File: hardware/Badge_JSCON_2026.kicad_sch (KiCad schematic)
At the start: 38 parts, among them J2 LCD, P1 USB_C_Plug_USB2.0, Q2 BC846, SW3 ON, U1 ESP32-S3-WROOM-1-N8, U2 BL8072CLTR33, U5 VGdd79S915N0S1

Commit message: feat(Hw):Update_Files
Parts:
- SW1, SW2, SW4, SW5, SW6, SW7: value (none) -> ~
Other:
- note added: "ESP32-C6"
- note removed: "ESP32-S3"

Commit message: feat(Hw):Init_Floorplan
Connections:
- net CS2: no longer names the net of U1.22 (IO14)
- net IO0: no longer names the net of U1.6 (IO6)
- net IO1: no longer names the net of U1.7 (IO7)
- net IO2: no longer names the net of U1.5 (IO5)
- net IRQ: no longer names the net of U1.12 (IO8)
- net MISO2: no longer names the net of U1.10 (IO17)
- net MOSI2: no longer names the net of U1.9 (IO16)
- net SCK2: no longer names the net of U1.8 (IO15)
- net SCL1: no longer names the net of U1.34 (IO41)
- net SDA1: no longer names the net of U1.35 (IO42)
- net SDN: no longer names the net of U1.4 (IO4)
- no-connect marks 5 -> 16
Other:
- company: (none) -> Electronic Cats
- title: (none) -> Badge JSCON 2026
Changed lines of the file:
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@@
 	(generator_version "9.0")
 	(paper "A3")
+	(title_block
+		(title "Badge JSCON 2026")
+		(rev "v1.0")
+		(company "Electronic Cats")
+		(comment 1 "Lizeth Gallegos Martínez")
+	)
 	(text "VGdd79S915N0S1\n"
 		(exclude_from_sim no)
@@
 	)
 	(no_connect
+		(at 36.83 45.72)
+	)
+	(no_connect
 		(at 36.83 71.12)
+	)
+	(no_connect
+		(at 36.83 48.26)
+	)
+	(no_connect
+		(at 77.47 68.58)
 	)
 	(no_connect
@@
 	)
 	(no_connect
+		(at 36.83 40.64)
+	)
+	(no_connect
+		(at 36.83 43.18)
+	)
+	(no_connect
+		(at 36.83 60.96)
+	)
+	(no_connect
+		(at 36.83 86.36)
+	)
+	(no_connect
+		(at 36.83 55.88)
+	)
+	(no_connect
+		(at 36.83 53.34)
+	)
+	(no_connect
 		(at 77.47 91.44)
 	)
@@
 		(at 331.47 68.58)
 	)
+	(no_connect
+		(at 36.83 50.8)
+	)
+	(no_connect
+		(at 77.47 71.12)
+	)
 	(wire
 		(pts
@@
 	(wire
 		(pts
-			(xy 81.28 68.58) (xy 77.47 68.58)
-		)
-		(stroke
-			(width 0)
-			(type default)
-		)
-	)
-	(wire
-		(pts
-			(xy 78.74 76.2) (xy 77.47 76.2)
+			(xy 80.01 76.2) (xy 77.47 76.2)
 		)
 		(stroke
@@
 	(wire
 		(pts
-			(xy 35.56 43.18) (xy 36.83 43.18)
-		)
-		(stroke
-			(width 0)
-			(type default)
-		)
-	)
-	(wire
-		(pts
 			(xy 340.36 55.88) (xy 340.36 58.42)
 		)
@@
 	(wire
 		(pts
-			(xy 36.83 86.36) (xy 33.02 86.36)
-		)
-		(stroke
-			(width 0)
-			(type default)
-		)
-	)
-	(wire
-		(pts
 			(xy 68.58 142.24) (xy 68.58 144.78)
 		)
@@
 	(wire
 		(pts
-			(xy 33.02 60.96) (xy 36.83 60.96)
-		)
-		(stroke
-			(width 0)
-			(type default)
-		)
-	)
-	(wire
-		(pts
 			(xy 156.21 57.15) (xy 152.019 57.15)
 		)
@@
 	(wire
 		(pts
-			(xy 35.56 45.72) (xy 36.83 45.72)
-		)
-		(stroke
-			(width 0)
-			(type default)
-		)
-	)
-	(wire
-		(pts
 			(xy 205.74 49.53) (xy 203.962 49.53)
 		)
@@
 	(wire
 		(pts
-			(xy 33.02 40.64) (xy 36.83 40.64)
-		)
-		(stroke
-			(width 0)
-			(type default)
-		)
-	)
-	(wire
-		(pts
 			(xy 33.02 66.04) (xy 36.83 66.04)
 		)
@@
 	(wire
 		(pts
-			(xy 81.28 71.12) (xy 77.47 71.12)
-		)
-		(stroke
-			(width 0)
-			(type default)
-		)
-	)
-	(wire
-		(pts
 			(xy 106.68 243.84) (xy 104.14 243.84)
 		)
@@
 	(wire
 		(pts
-			(xy 35.56 48.26) (xy 36.83 48.26)
-		)
-		(stroke
-			(width 0)
-			(type default)
-		)
-	)
-	(wire
-		(pts
 			(xy 128.27 68.834) (xy 128.27 72.644)
 		)
@@
 	(wire
 		(pts
-			(xy 33.02 50.8) (xy 36.83 50.8)
-		)
-		(stroke
-			(width 0)
-			(type default)
-		)
-	)
-	(wire
-		(pts
 			(xy 59.69 144.78) (xy 60.96 144.78)
 		)
@@
 	(wire
 		(pts
-			(xy 33.02 55.88) (xy 36.83 55.88)
-		)
-		(stroke
-			(width 0)
-			(type default)
-		)
-	)
-	(wire
-		(pts
 			(xy 44.45 176.53) (xy 44.45 177.292)
 		)
@@
 	(wire
 		(pts
-			(xy 33.02 53.34) (xy 36.83 53.34)
-		)
-		(stroke
-			(width 0)
-			(type default)
-		)
-	)
-	(wire
-		(pts
 			(xy 25.4 33.02) (xy 36.83 33.02)
 		)
@@
 	(wire
 		(pts
-			(xy 78.74 73.66) (xy 77.47 73.66)
+			(xy 80.01 73.66) (xy 77.47 73.66)
 		)
 		(stroke
@@
 		)
 	)
-	(label "SCK2"
-		(at 33.02 50.8 180)
-		(effects
-			(font
-				(size 1.27 1.27)
-			)
-			(justify right bottom)
-		)
-	)
 	(label "BUSY"
-		(at 78.74 76.2 0)
+		(at 80.01 76.2 0)
 		(effects
 			(font
@@
 		)
 	)
-	(label "CS2"
-		(at 33.02 86.36 180)
-		(effects
-			(font
-				(size 1.27 1.27)
-			)
-			(justify right bottom)
-		)
-	)
 	(label "RIGHT"
 		(at 201.93 49.53 180)
@@
 		)
 	)
-	(label "IO0"
-		(at 35.56 45.72 180)
-		(effects
-			(font
-				(size 1.27 1.27)
-			)
-			(justify right bottom)
-		)
-	)
 	(label "MISO"
 		(at 81.28 83.82 0)
@@
 	)
 	(label "UP"
-		(at 78.74 73.66 0)
+		(at 80.01 73.66 0)
 		(effects
 			(font
@@
 		)
 	)
-	(label "IRQ"
-		(at 33.02 60.96 180)
-		(effects
-			(font
-				(size 1.27 1.27)
-			)
-			(justify right bottom)
-		)
-	)
 	(label "SCL"
 		(at 104.14 246.38 180)
@@
 		)
 	)
-	(label "MOSI2"
-		(at 33.02 53.34 180)
-		(effects
-			(font
-				(size 1.27 1.27)
-			)
-			(justify right bottom)
-		)
-	)
 	(label "DOWN"
 		(at 78.74 63.5 0)
@@
 		)
 	)
-	(label "IO1"
-		(at 35.56 48.26 180)
-		(effects
-			(font
-				(size 1.27 1.27)
-			)
-			(justify right bottom)
-		)
-	)
-	(label "SDN"
-		(at 33.02 40.64 180)
-		(effects
-			(font
-				(size 1.27 1.27)
-			)
-			(justify right bottom)
-		)
-	)
 	(label "SDA"
 		(at 35.56 243.84 180)
@@
 		)
 	)
-	(label "IO2"
-		(at 35.56 43.18 180)
-		(effects
-			(font
-				(size 1.27 1.27)
-			)
-			(justify right bottom)
-		)
-	)
-	(label "MISO2"
-		(at 33.02 55.88 180)
-		(effects
-			(font
-				(size 1.27 1.27)
-			)
-			(justify right bottom)
-		)
-	)
 	(label "D-"
 		(at 63.246 149.86 0)
@@
 		)
 	)
-	(label "SDA1"
-		(at 81.28 68.58 0)
-		(effects
-			(font
-				(size 1.27 1.27)
-			)
-			(justify left bottom)
-		)
-	)
 	(label "D-"
 		(at 33.02 63.5 180)
@@
 		(effects
 			(font
-				(size 1.27 1.27)
-			)
-			(justify left bottom)
-		)
-	)
-	(label "SCL1"
-		(at 81.28 71.12 0)
-		(effects
-			(font

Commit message: feat(Hw):Init_Route
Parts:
- removed R17, R18: 4.7K, Resistor_SMD:R_0603_1608Metric, symbol Device:R
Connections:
- net SCL renamed SPI_SCLK
- net SDA renamed SPI_MOSI
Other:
- moved on the sheet: R3

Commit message: feat(Hw):Update_Route
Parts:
- C10, C11, C4, C5, C8, C9: LCSC# C478888 -> C14663
- C13, C2, C3, C6, C7: LCSC# C85713 -> C96446
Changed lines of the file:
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@@
 			)
 		)
-		(property "LCSC#" "C478888 "
+		(property "LCSC#" "C14663"
 			(at 210.82 36.83 0)
 			(effects
@@
 			)
 		)
-		(property "LCSC#" "C85713"
+		(property "LCSC#" "C96446"
 			(at 128.27 75.184 0)
 			(effects
@@
 			)
 		)
-		(property "LCSC#" "C85713"
+		(property "LCSC#" "C96446"
 			(at 119.38 75.184 0)
 			(effects
@@
 			)
 		)
-		(property "LCSC#" "C85713"
+		(property "LCSC#" "C96446"
 			(at 148.59 154.94 0)
 			(effects
@@
 			)
 		)
-		(property "LCSC#" "C85713"
+		(property "LCSC#" "C96446"
 			(at 168.91 154.94 0)
 			(effects
@@
 			)
 		)
-		(property "LCSC#" "C478888 "
+		(property "LCSC#" "C14663"
 			(at 158.75 57.15 0)
 			(effects
@@
 			)
 		)
-		(property "LCSC#" "C478888 "
+		(property "LCSC#" "C14663"
 			(at 157.353 73.152 0)
 			(effects
@@
 			)
 		)
-		(property "LCSC#" "C85713"
+		(property "LCSC#" "C96446"
 			(at 288.29 72.39 0)
 			(effects
@@
 			)
 		)
-		(property "LCSC#" "C478888 "
+		(property "LCSC#" "C14663"
 			(at 212.09 86.36 0)
 			(effects
@@
 			)
 		)
-		(property "LCSC#" "C478888 "
+		(property "LCSC#" "C14663"
 			(at 210.82 69.85 0)
 			(effects
@@
 			)
 		)
-		(property "LCSC#" "C478888 "
+		(property "LCSC#" "C14663"
 			(at 210.82 53.34 0)
 			(effects

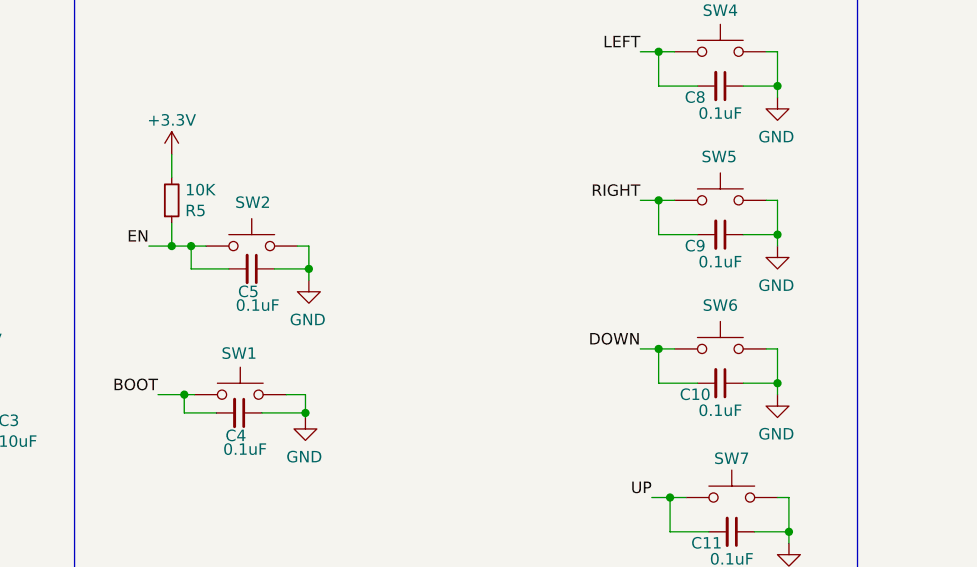
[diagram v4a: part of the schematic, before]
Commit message: fix: resistor 10k price
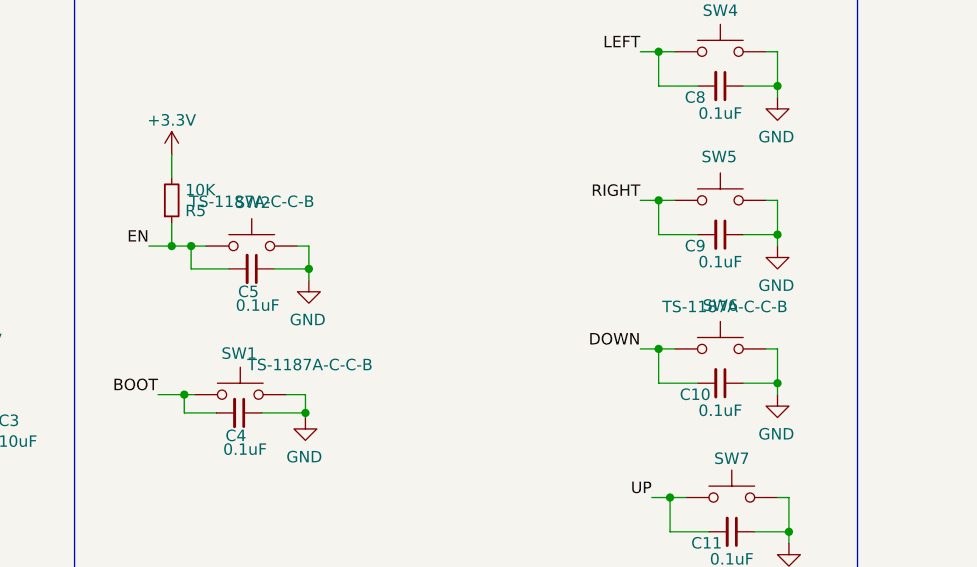
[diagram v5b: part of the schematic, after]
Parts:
- AE1: Category (none) -> Electronic Components / Antennas; LCSC# C530661 -> (none); lcsc# (none) -> C530661; manf# (none) -> KH-SMA-KE8-G
- C1: Category (none) -> Electronic Components / Capacitors; LCSC# C15849 -> (none); lcsc# (none) -> C15849; manf# (none) -> CL10A105KB8NNNC
- C10, C11, C4, C5, C8, C9: Category (none) -> Electronic Components / Capacitors; LCSC# C14663 -> (none); lcsc# (none) -> C478888; manf# (none) -> C0603B104K500NT
- C12: Category (none) -> Electronic Components / Capacitors; LCSC# C14663 -> (none); lcsc# (none) -> C14663; manf# (none) -> CC0603KRX7R9BB104
- C13, C2, C3, C6, C7: Category (none) -> Electronic Components / Capacitors; LCSC# C96446 -> (none); lcsc# (none) -> C85713; manf# (none) -> CL10A106MP8NNNC
- F1: Category (none) -> Electronic Components / Fuses & Protection; LCSC# C182438 -> (none); lcsc# (none) -> C182438; manf# (none) -> 06D0750D
- J2: Category (none) -> Electronic Components / Connectors; LCSC# C262583 -> (none); lcsc# (none) -> C262583; manf# (none) -> AFC07-S10ECA-00
- P1: Category (none) -> Electronic Components / Connectors; LCSC# C393939 -> (none); lcsc# (none) -> C393939; manf# (none) -> TYPE-C16PIN
- Q2: Category (none) -> Electronic Components / Transistors; LCSC# C49238181 -> (none); lcsc# (none) -> C49238181; manf# (none) -> BC849C
- R1, R2: Category (none) -> Electronic Components / Resistors; LCSC# C113390 -> (none); lcsc# (none) -> C113390; manf# (none) -> WR06X5101FTL
- R12, R3, R5, R8: Category (none) -> Electronic Components / Resistors; LCSC# C2930027 -> (none); lcsc# (none) -> C54920960; manf# (none) -> HRC0603J103 ENTN
- R13: Category (none) -> Electronic Components / Resistors; LCSC# C2907002 -> (none); lcsc# (none) -> C2907002; manf# (none) -> FRC0603F1001TS
- R14: Category (none) -> Electronic Components / Resistors; LCSC# C2933216 -> (none); lcsc# (none) -> C2933216; manf# (none) -> FRC0603F3R90TS
- SW1, SW2, SW4, SW5, SW6, SW7: value ~ -> TS-1187A-C-C-B; Category (none) -> Electronic Components / Switches; LCSC# C318889 -> (none); lcsc# (none) -> C318889; manf# (none) -> TS-1187A-C-C-B
- SW3: Category (none) -> Electronic Components / Switches; LCSC# C431540 -> (none); lcsc# (none) -> C431540; manf# (none) -> MSK12C02
- U1: Category (none) -> Electronic Components / Integrated Circuits; lcsc# (none) -> C2913198; manf# ESP32-S3-WROOM-1-N8 -> ESP32-S3-WROOM-1-N8
- U2: Category (none) -> Electronic Components / Integrated Circuits; LCSC# C843780 -> (none); lcsc# (none) -> C843780; manf# (none) -> BL8072CLTR33
- U5: Category (none) -> Electronic Components / Integrated Circuits; LCSC# C2848401 -> (none); lcsc# (none) -> C2848401; manf# (none) -> VGdd79S915N0S1
